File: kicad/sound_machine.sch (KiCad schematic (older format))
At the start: 3 parts

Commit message: Speaker
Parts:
- added LS?: Speaker, symbol Speaker
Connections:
- net labels added: +5V, GND, SCL, SDA
- wire segments 0 -> 14
- no-connect marks 0 -> 6
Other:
- moved on the sheet: U?
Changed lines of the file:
@@
 LIBS:valves
 LIBS:sound_machine
+LIBS:sound_machine-cache
 EELAYER 25 0
 EELAYER END
@@
 L DFPlayerMini U?
 U 1 1 59A0400A
-P 5725 2525
-F 0 "U?" H 5725 3025 60  0000 C CNN
-F 1 "DFPlayerMini" H 5725 1975 60  0000 C CNN
-F 2 "" H 5775 2125 60  0001 C CNN
-F 3 "" H 5775 2125 60  0001 C CNN
-	1    5725 2525
+P 8275 2375
+F 0 "U?" H 8275 2875 60  0000 C CNN
+F 1 "DFPlayerMini" H 8275 1825 60  0000 C CNN
+F 2 "" H 8325 1975 60  0001 C CNN
+F 3 "" H 8325 1975 60  0001 C CNN
+	1    8275 2375
 	1    0    0    -1
 $EndComp
@@
 	1    0    0    -1
 $EndComp
+$Comp
+L Speaker LS?
+U 1 1 59A04FC9
+P 7075 2575
+F 0 "LS?" H 7125 2800 50  0000 R CNN
+F 1 "Speaker" H 7125 2725 50  0000 R CNN
+F 2 "" H 7075 2375 50  0001 C CNN
+F 3 "" H 7065 2525 50  0001 C CNN
+	1    7075 2575
+	-1   0    0    -1
+$EndComp
+Wire Wire Line
+	7675 2525 7275 2525
+Wire Wire Line
+	7275 2525 7275 2575
+Wire Wire Line
+	7675 2725 7275 2725
+Wire Wire Line
+	7275 2725 7275 2675
+$Comp
+L GND #PWR?
+U 1 1 59A05105
+P 7600 2900
+F 0 "#PWR?" H 7600 2650 50  0001 C CNN
+F 1 "GND" H 7600 2750 50  0000 C CNN
+F 2 "" H 7600 2900 50  0001 C CNN
+F 3 "" H 7600 2900 50  0001 C CNN
+	1    7600 2900
+	1    0    0    -1
+$EndComp
+Wire Wire Line
+	7600 2900 7600 2625
+Wire Wire Line
+	7600 2625 7675 2625
+NoConn ~ 7675 2325
+NoConn ~ 7675 2425
+NoConn ~ 8875 2125
+NoConn ~ 8875 2225
+NoConn ~ 8875 2525
+NoConn ~ 8875 2725
+$Comp
+L GND #PWR?
+U 1 1 59A0515F
+P 9125 2875
+F 0 "#PWR?" H 9125 2625 50  0001 C CNN
+F 1 "GND" H 9125 2725 50  0000 C CNN
+F 2 "" H 9125 2875 50  0001 C CNN
+F 3 "" H 9125 2875 50  0001 C CNN
+	1    9125 2875
+	1    0    0    -1
+$EndComp
+Wire Wire Line
+	8875 2625 9125 2625
+Wire Wire Line
+	9125 2625 9125 2875
+$Comp
+L +5V #PWR?
+U 1 1 59A05201
+P 7500 1900
+F 0 "#PWR?" H 7500 1750 50  0001 C CNN
+F 1 "+5V" H 7500 2040 50  0000 C CNN
+F 2 "" H 7500 1900 50  0001 C CNN
+F 3 "" H 7500 1900 50  0001 C CNN
+	1    7500 1900
+	1    0    0    -1
+$EndComp
+Wire Wire Line
+	7675 2025 7500 2025
+Wire Wire Line
+	7500 2025 7500 1900
+Text GLabel 4100 3400 2    60   Input ~ 0
+SDA
+Text GLabel 4100 3500 2    60   Input ~ 0
+SCL
+Wire Wire Line
+	4100 3400 3950 3400
+Wire Wire Line
+	3950 3500 4100 3500
+Text GLabel 5375 3975 0    60   Input ~ 0
+SDA
+Text GLabel 5375 3875 0    60   Input ~ 0
+SCL
+$Comp
+L GND #PWR?
+U 1 1 59A053B4
+P 4975 3825
+F 0 "#PWR?" H 4975 3575 50  0001 C CNN
+F 1 "GND" H 4975 3675 50  0000 C CNN
+F 2 "" H 4975 3825 50  0001 C CNN
+F 3 "" H 4975 3825 50  0001 C CNN
+	1    4975 3825
+	1    0    0    -1
+$EndComp
+Wire Wire Line
+	5375 3775 4975 3775
+Wire Wire Line
+	4975 3775 4975 3825
 $EndSCHEMATC

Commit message: Nano connections
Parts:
- removed U?: ATMEGA328P-AU, TQFP32, symbol ATMEGA328P-AU
- added A1: Arduino_Nano, symbol Arduino_Nano
- added J1: Conn_01x02, symbol Conn_01x02
- added J2, J3: Conn_01x15, symbol Conn_01x15
- added J4, J6, J7, J8: TEST_1P, symbol TEST_1P
- added J5: Audio-Jack-3, symbol Audio-Jack-3
- added R1: 330R, symbol R
- added R2: 1K, symbol R
- gave numbers to parts that had none: 3
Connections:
- net labels added: +3.3V, A0, A1, A2, A3, A6, A7, AHREF, D10, D11, D12, D13, D2, D3, D4, D5, D6, D7, D8, D9, RST, RX0, TX1, VIN
- wire segments 14 -> 28
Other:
- moved on the sheet: LS1, U1, U2

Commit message: Schematic done
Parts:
- removed A1: Arduino_Nano, symbol Arduino_Nano
- J1, LS1: footprint (none) -> Pin_Headers:Pin_Header_Straight_1x02_Pitch2.54mm
- J2, J3: footprint (none) -> Pin_Headers:Pin_Header_Straight_1x15_Pitch2.54mm
- J4, J6, J7, J8: footprint (none) -> Measurement_Points:Measurement_Point_Round-SMD-Pad_Small
- J5: footprint (none) -> Connectors:BARREL_JACK
- R1, R2: footprint (none) -> Resistors_SMD:R_0805_HandSoldering
- U1: footprint (none) -> Pin_Headers:Pin_Header_Straight_1x08_Pitch2.54mm
- U2: footprint (none) -> Socket_Strips:Socket_Strip_Straight_2x08_Pitch2.54mm
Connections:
- wire segments 28 -> 25
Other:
- moved on the sheet: J1, J2, J3

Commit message: Basic layout
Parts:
- U2: footprint Socket_Strips:Socket_Strip_Straight_2x08_Pitch2.54mm -> sound_machine:DFPlayerMini
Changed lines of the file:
@@
 LIBS:valves
 LIBS:sound_machine
-LIBS:arduino_nano
 LIBS:sound_machine-cache
 EELAYER 25 0
@@
 F 0 "U2" H 8625 5350 60  0000 C CNN
 F 1 "DFPlayerMini" H 8625 4300 60  0000 C CNN
-F 2 "Socket_Strips:Socket_Strip_Straight_2x08_Pitch2.54mm" H 8675 4450 60  0001 C CNN
+F 2 "sound_machine:DFPlayerMini" H 8675 4450 60  0001 C CNN
 F 3 "" H 8675 4450 60  0001 C CNN
 	1    8625 4850

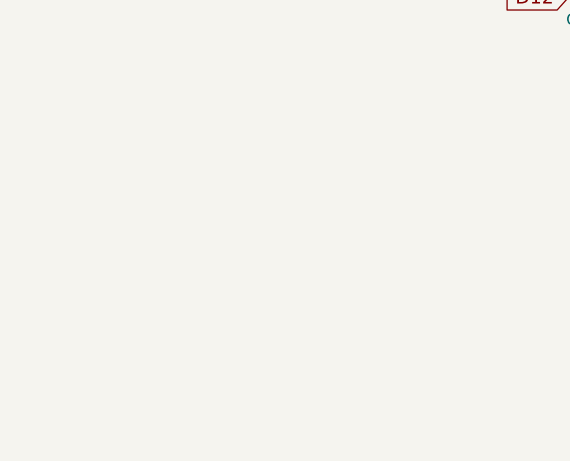
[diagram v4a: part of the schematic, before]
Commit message: Mounting holes
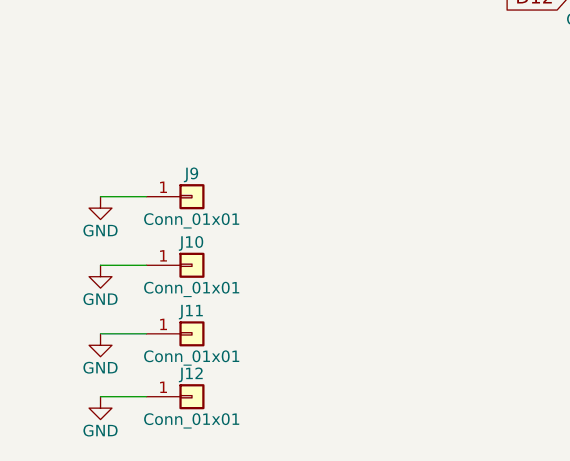
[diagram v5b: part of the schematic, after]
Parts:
- added J10, J11, J12, J9: Conn_01x01, Mounting_Holes:MountingHole_2.2mm_M2_Pad, symbol Conn_01x01
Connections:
- net GND: now also J10.1 (Pin_1), J11.1 (Pin_1), J12.1 (Pin_1), J9.1 (Pin_1)
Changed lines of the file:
@@
 Wire Wire Line
 	1875 3650 2075 3650
+$Comp
+L Conn_01x01 J9
+U 1 1 5A3DAE79
+P 2500 5300
+F 0 "J9" H 2500 5400 50  0000 C CNN
+F 1 "Conn_01x01" H 2500 5200 50  0000 C CNN
+F 2 "Mounting_Holes:MountingHole_2.2mm_M2_Pad" H 2500 5300 50  0001 C CNN
+F 3 "" H 2500 5300 50  0001 C CNN
+	1    2500 5300
+	1    0    0    -1
+$EndComp
+$Comp
+L Conn_01x01 J10
+U 1 1 5A3DAFB0
+P 2500 5600
+F 0 "J10" H 2500 5700 50  0000 C CNN
+F 1 "Conn_01x01" H 2500 5500 50  0000 C CNN
+F 2 "Mounting_Holes:MountingHole_2.2mm_M2_Pad" H 2500 5600 50  0001 C CNN
+F 3 "" H 2500 5600 50  0001 C CNN
+	1    2500 5600
+	1    0    0    -1
+$EndComp
+$Comp
+L Conn_01x01 J11
+U 1 1 5A3DAFF9
+P 2500 5900
+F 0 "J11" H 2500 6000 50  0000 C CNN
+F 1 "Conn_01x01" H 2500 5800 50  0000 C CNN
+F 2 "Mounting_Holes:MountingHole_2.2mm_M2_Pad" H 2500 5900 50  0001 C CNN
+F 3 "" H 2500 5900 50  0001 C CNN
+	1    2500 5900
+	1    0    0    -1
+$EndComp
+$Comp
+L Conn_01x01 J12
+U 1 1 5A3DB091
+P 2500 6175
+F 0 "J12" H 2500 6275 50  0000 C CNN
+F 1 "Conn_01x01" H 2500 6075 50  0000 C CNN
+F 2 "Mounting_Holes:MountingHole_2.2mm_M2_Pad" H 2500 6175 50  0001 C CNN
+F 3 "" H 2500 6175 50  0001 C CNN
+	1    2500 6175
+	1    0    0    -1
+$EndComp
+$Comp
+L GND #PWR012
+U 1 1 5A3DB0F5
+P 2100 5300
+F 0 "#PWR012" H 2100 5050 50  0001 C CNN
+F 1 "GND" H 2100 5150 50  0000 C CNN
+F 2 "" H 2100 5300 50  0001 C CNN
+F 3 "" H 2100 5300 50  0001 C CNN
+	1    2100 5300
+	1    0    0    -1
+$EndComp
+$Comp
+L GND #PWR013
+U 1 1 5A3DB155
+P 2100 5600
+F 0 "#PWR013" H 2100 5350 50  0001 C CNN
+F 1 "GND" H 2100 5450 50  0000 C CNN
+F 2 "" H 2100 5600 50  0001 C CNN
+F 3 "" H 2100 5600 50  0001 C CNN
+	1    2100 5600
+	1    0    0    -1
+$EndComp
+$Comp
+L GND #PWR014
+U 1 1 5A3DB193
+P 2100 5900
+F 0 "#PWR014" H 2100 5650 50  0001 C CNN
+F 1 "GND" H 2100 5750 50  0000 C CNN
+F 2 "" H 2100 5900 50  0001 C CNN
+F 3 "" H 2100 5900 50  0001 C CNN
+	1    2100 5900
+	1    0    0    -1
+$EndComp
+$Comp
+L GND #PWR015
+U 1 1 5A3DB1D1
+P 2100 6175
+F 0 "#PWR015" H 2100 5925 50  0001 C CNN
+F 1 "GND" H 2100 6025 50  0000 C CNN
+F 2 "" H 2100 6175 50  0001 C CNN
+F 3 "" H 2100 6175 50  0001 C CNN
+	1    2100 6175
+	1    0    0    -1
+$EndComp
+Wire Wire Line
+	2100 5300 2300 5300
+Wire Wire Line
+	2300 5600 2100 5600
+Wire Wire Line
+	2300 5900 2100 5900
+Wire Wire Line
+	2100 6175 2300 6175
 $EndSCHEMATC

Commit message: Nano expansion
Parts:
- added J13, J14, J15, J16, J17, J18: Conn_01x15, Pin_Headers:Pin_Header_Straight_1x15_Pitch2.54mm, symbol Conn_01x15
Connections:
- net +3V3: now also J16.14 (Pin_14), J17.14 (Pin_14), J18.14 (Pin_14)
- net +5V: now also J16.4 (Pin_4), J17.4 (Pin_4), J18.4 (Pin_4)
- net A0: now also J16.12 (Pin_12), J17.12 (Pin_12), J18.12 (Pin_12)
- net A1: now also J16.11 (Pin_11), J17.11 (Pin_11), J18.11 (Pin_11)
- net A2: now also J16.10 (Pin_10), J17.10 (Pin_10), J18.10 (Pin_10)
- net A3: now also J16.9 (Pin_9), J17.9 (Pin_9), J18.9 (Pin_9)
- net A6: now also J16.6 (Pin_6), J17.6 (Pin_6), J18.6 (Pin_6)
- net A7: now also J16.5 (Pin_5), J17.5 (Pin_5), J18.5 (Pin_5)
- net AHREF: now also J16.13 (Pin_13), J17.13 (Pin_13), J18.13 (Pin_13)
- net D10: now also J13.13 (Pin_13), J14.13 (Pin_13), J15.13 (Pin_13)
- net D11: now also J13.14 (Pin_14), J14.14 (Pin_14), J15.14 (Pin_14)
- net D12: now also J13.15 (Pin_15), J14.15 (Pin_15), J15.15 (Pin_15)
- net D13: now also J16.15 (Pin_15), J17.15 (Pin_15), J18.15 (Pin_15)
- net D2: now also J13.5 (Pin_5), J14.5 (Pin_5), J15.5 (Pin_5)
- net D3: now also J13.6 (Pin_6), J14.6 (Pin_6), J15.6 (Pin_6)
- net D4: now also J13.7 (Pin_7), J14.7 (Pin_7), J15.7 (Pin_7)
- net D5: now also J13.8 (Pin_8), J14.8 (Pin_8), J15.8 (Pin_8)
- net D6: now also J13.9 (Pin_9), J14.9 (Pin_9), J15.9 (Pin_9)
- net D7: now also J13.10 (Pin_10), J14.10 (Pin_10), J15.10 (Pin_10)
- net D8: now also J13.11 (Pin_11), J14.11 (Pin_11), J15.11 (Pin_11)
- net D9: now also J13.12 (Pin_12), J14.12 (Pin_12), J15.12 (Pin_12)
- net GND: now also J13.4 (Pin_4), J14.4 (Pin_4), J15.4 (Pin_4), J16.2 (Pin_2), J17.2 (Pin_2), J18.2 (Pin_2)
- net RST: now also J13.3 (Pin_3), J14.3 (Pin_3), J15.3 (Pin_3), J16.3 (Pin_3), J17.3 (Pin_3), J18.3 (Pin_3)
- net RX0: now also J13.2 (Pin_2), J14.2 (Pin_2), J15.2 (Pin_2)
- net SCL: now also J16.7 (Pin_7), J17.7 (Pin_7), J18.7 (Pin_7)
- net SDA: now also J16.8 (Pin_8), J17.8 (Pin_8), J18.8 (Pin_8)
- net TX1: now also J13.1 (Pin_1), J14.1 (Pin_1), J15.1 (Pin_1)
- net VIN: now also J16.1 (Pin_1), J17.1 (Pin_1), J18.1 (Pin_1)
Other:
- moved on the sheet: J1, J2, J3, J4, J5, J6, J7, J8, LS1, R1, R2, U1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

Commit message: Connected
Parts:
- removed J4, J6, J7, J8: TEST_1P, Measurement_Points:Measurement_Point_Round-SMD-Pad_Small, symbol TEST_1P
- added J19, J20, J21, J22, J23, J24, J25, J26: Conn_02x25_Counter_Clockwise, Pin_Headers:Pin_Header_Straight_2x25_Pitch2.54mm, symbol Conn_02x25_Counter_Clockwise
- added J4, J6: Conn_01x08, Pin_Headers:Pin_Header_Straight_1x08_Pitch2.54mm, symbol Conn_01x08
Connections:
- net +5V: now also J4.1 (Pin_1)
- net GND: now also J4.7 (Pin_7), J6.7 (Pin_7)
- net RST: no longer J16.3 (Pin_3), J17.3 (Pin_3), J18.3 (Pin_3), J3.3 (Pin_3)
- net RX0: now also J4.3 (Pin_3)
- net at U2.11 (IO2): now also J6.6 (Pin_6)
- net at U2.12 (ADKEY1): now also J6.5 (Pin_5)
- net at U2.13 (ADKEY2): now also J6.4 (Pin_4)
- net at U2.14 (USB+): now also J6.3 (Pin_3)
- net at U2.15 (USB-): now also J6.2 (Pin_2)
- net at U2.16 (BUSY): now also J6.1 (Pin_1)
- net at R2.1, U2.2 (RX): now also J4.2 (Pin_2)
- net at J5.2, U2.4 (DAC_R): now also J4.4 (Pin_4)
- net at J5.1, U2.5 (DAC_L): now also J4.5 (Pin_5)
- net at LS1.1, U2.6 (SPK_1): now also J4.6 (Pin_6)
- net at LS1.2, U2.8 (SPK_2): now also J4.8 (Pin_8)
- net at U2.9 (IO1): now also J6.8 (Pin_8)
- new net RESET: J16.3 (Pin_3), J17.3 (Pin_3), J18.3 (Pin_3), J3.3 (Pin_3)
- no-connect marks 6 -> 3
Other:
- moved on the sheet: J1, J10, J11, J12, J13, J14, J15, J16, J17, J18, J2, J3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

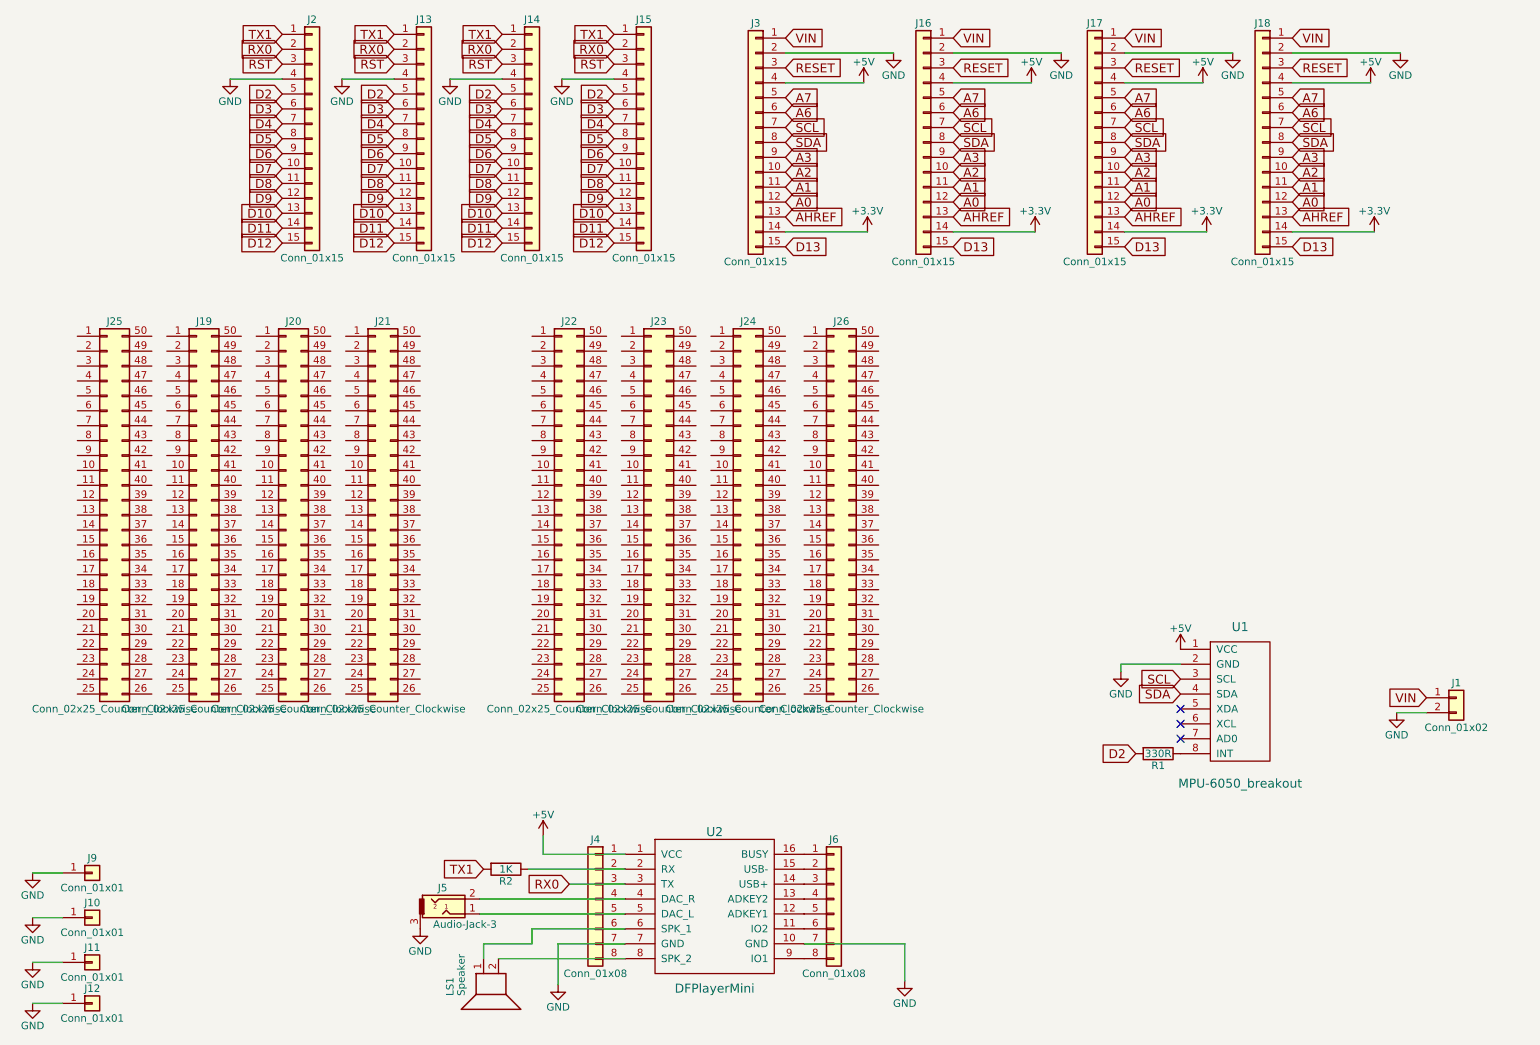
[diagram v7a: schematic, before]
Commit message: Smaller board
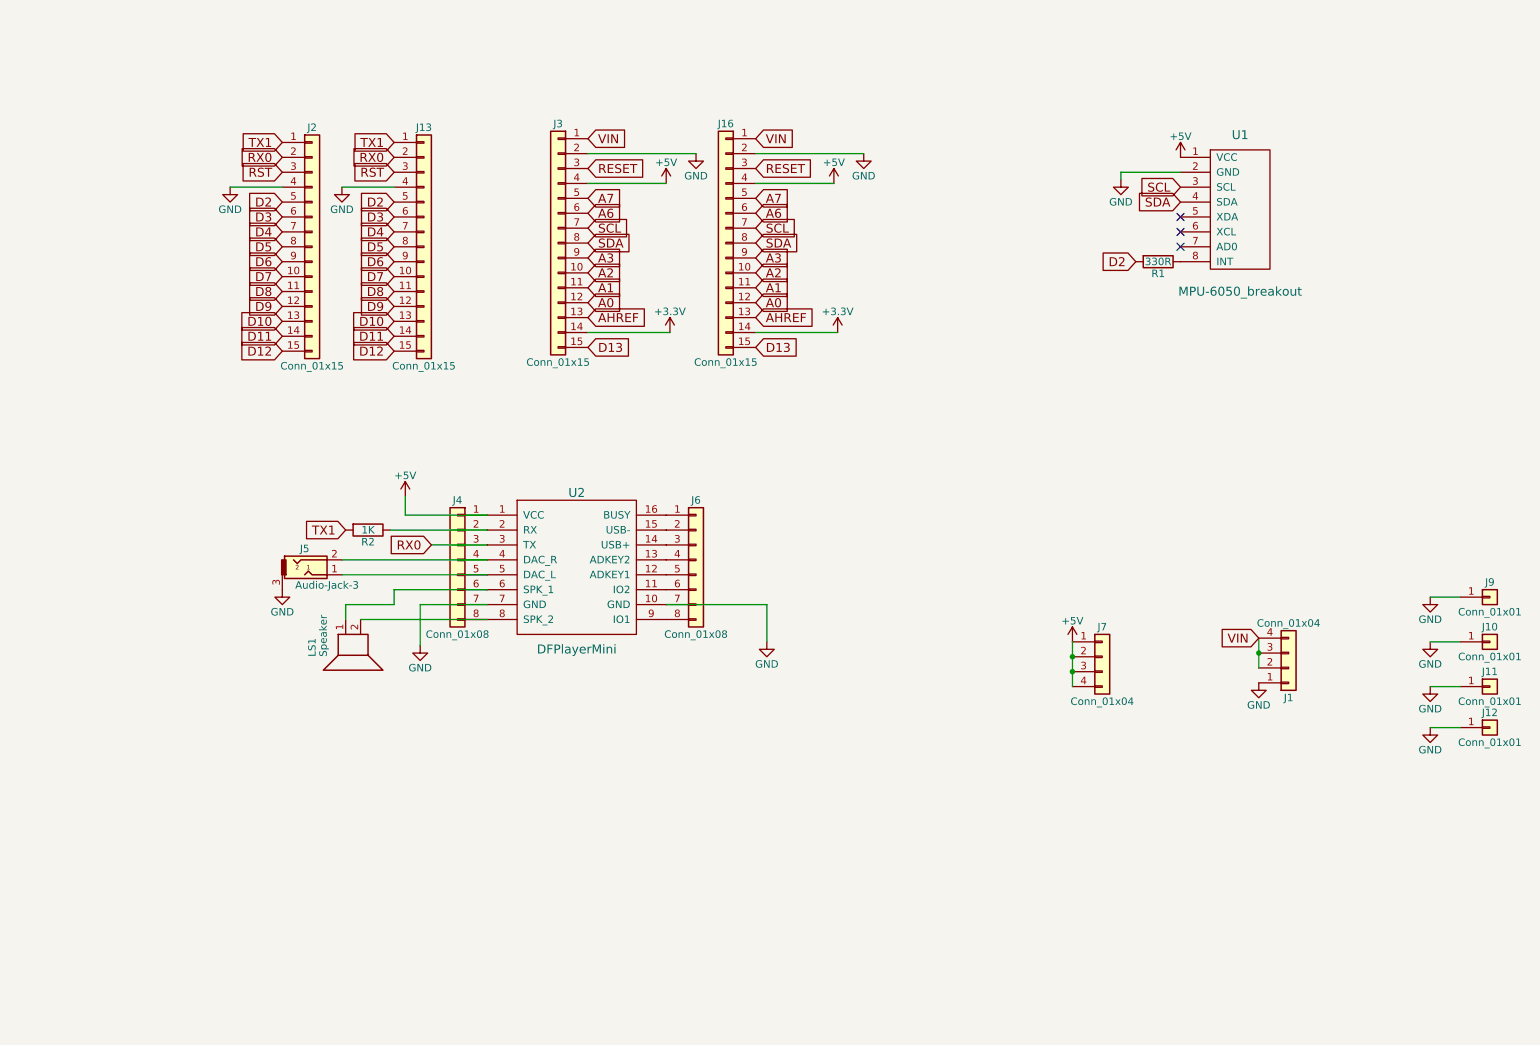
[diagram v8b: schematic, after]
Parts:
- removed J1: Conn_01x02, Pin_Headers:Pin_Header_Straight_1x02_Pitch2.54mm, symbol Conn_01x02
- removed J14, J15, J17, J18: Conn_01x15, Pin_Headers:Pin_Header_Straight_1x15_Pitch2.54mm, symbol Conn_01x15
- removed J19, J20, J21, J22, J23, J24, J25, J26: Conn_02x25_Counter_Clockwise, Pin_Headers:Pin_Header_Straight_2x25_Pitch2.54mm, symbol Conn_02x25_Counter_Clockwise
- added J1, J7: Conn_01x04, Pin_Headers:Pin_Header_Straight_1x04_Pitch2.54mm, symbol Conn_01x04
- J10, J11, J12, J9: footprint Mounting_Holes:MountingHole_2.2mm_M2_Pad -> Mounting_Holes:MountingHole_3.2mm_M3_Pad
- U1: footprint Pin_Headers:Pin_Header_Straight_1x08_Pitch2.54mm -> sound_machine:MPU-6050
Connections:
- net +5V: now also J7.1 (Pin_1), J7.2 (Pin_2), J7.3 (Pin_3), J7.4 (Pin_4)
- net GND: now also J1.1 (Pin_1)
- net VIN: now also J1.2 (Pin_2), J1.3 (Pin_3), J1.4 (Pin_4)
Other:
- moved on the sheet: J10, J11, J12, J13, J16, J2, J3, J4, J5, J6, J9, LS1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
